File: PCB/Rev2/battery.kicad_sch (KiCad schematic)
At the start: 1 part, among them J2 Conn_01x04

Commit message: layout and  Routing adjustment
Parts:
- removed J2: Conn_01x04, 4ms_Connector:Pins_1x04_2.54mm_TH_SWD, symbol PCM_4ms_Connector:Conn_01x04
- added BT1, BT2: Battery, Connector_Molex:Molex_Panelmate_53780-0270_1x02-1MP_P1.25mm_Horizontal, symbol Device:Battery
- added C21: 10u, Capacitor_SMD:C_0402_1005Metric, symbol Device:C
- added C22: 22u, Capacitor_SMD:C_0603_1608Metric, symbol Device:C
- added L5: 2.2uH, Inductor_SMD:L_Changjiang_FNR252012S, symbol Device:L
- added R6: 1k, PCM_Resistor_SMD_AKL:R_0402_1005Metric, symbol Device:R
- added R7: 800k, PCM_Resistor_SMD_AKL:R_0603_1608Metric, symbol Device:R
- added R8: 10k, PCM_Resistor_SMD_AKL:R_0402_1005Metric, symbol Device:R
- added R9: 2M, PCM_Resistor_SMD_AKL:R_0603_1608Metric, symbol Device:R
- added U2: ETA6093, Package_TO_SOT_SMD:SOT-23-5, symbol ETA6093:ETA6093
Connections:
- net CHRG: now also R6.2, R8.1
- net GND: now also BT1.2 (-), BT2.2 (-), C21.2, C22.2, R9.2, U2.2 (GND)
- net VBUS: now also C22.1, R8.2, U2.1 (OUT)
- new net: L5.2, U2.5 (SW)
- new net: R6.1, U2.3 (LED)
- new net +BATT: BT1.1 (+), BT2.1 (+), C21.1, L5.1, R7.1, U2.4 (BAT)
- new net ADC: R7.2, R9.1
- no-connect marks 1 -> 0

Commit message: Change battery connector
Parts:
- BT1, BT2: footprint Connector_Molex:Molex_Panelmate_53780-0270_1x02-1MP_P1.25mm_Horizontal -> Connector_Molex:Molex_PicoBlade_53261-0271_1x02-1MP_P1.25mm_Horizontal
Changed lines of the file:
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@@
 			)
 		)
-		(property "Footprint" "Connector_Molex:Molex_Panelmate_53780-0270_1x02-1MP_P1.25mm_Horizontal"
+		(property "Footprint" "Connector_Molex:Molex_PicoBlade_53261-0271_1x02-1MP_P1.25mm_Horizontal"
 			(at 116.84 65.786 90)
 			(effects
@@
 			)
 		)
-		(property "Footprint" "Connector_Molex:Molex_Panelmate_53780-0270_1x02-1MP_P1.25mm_Horizontal"
+		(property "Footprint" "Connector_Molex:Molex_PicoBlade_53261-0271_1x02-1MP_P1.25mm_Horizontal"
 			(at 109.22 67.056 90)
 			(effects

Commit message: drc
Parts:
- removed BT1, BT2: Battery, Connector_Molex:Molex_PicoBlade_53261-0271_1x02-1MP_P1.25mm_Horizontal, symbol Device:Battery
- removed C21: 10u, Capacitor_SMD:C_0402_1005Metric, symbol Device:C
- removed C22: 22u, Capacitor_SMD:C_0603_1608Metric, symbol Device:C
- removed L5: 2.2uH, Inductor_SMD:L_Changjiang_FNR252012S, symbol Device:L
- removed R6: 1k, PCM_Resistor_SMD_AKL:R_0402_1005Metric, symbol Device:R
- removed R7: 800k, PCM_Resistor_SMD_AKL:R_0603_1608Metric, symbol Device:R
- removed R8: 10k, PCM_Resistor_SMD_AKL:R_0402_1005Metric, symbol Device:R
- removed R9: 2M, PCM_Resistor_SMD_AKL:R_0603_1608Metric, symbol Device:R
- removed U2: ETA6093, Package_TO_SOT_SMD:SOT-23-5, symbol ETA6093:ETA6093
- added BT3: Battery, Connector_Molex:Molex_PicoBlade_53261-0271_1x02-1MP_P1.25mm_Horizontal, symbol Device:Battery
- added C26: 20u, Capacitor_SMD:C_0402_1005Metric, symbol Device:C
- added C27: 10u, Capacitor_SMD:C_0402_1005Metric, symbol Device:C
- added C28: 22u, Capacitor_SMD:C_0603_1608Metric, symbol Device:C
- added L6: 2.2uH, Inductor_SMD:L_Changjiang_FNR252012S, symbol Device:L
- added R11: 1k, PCM_Resistor_SMD_AKL:R_0402_1005Metric, symbol Device:R
- added R12: 800k, PCM_Resistor_SMD_AKL:R_0603_1608Metric, symbol Device:R
- added R13: 2M, PCM_Resistor_SMD_AKL:R_0603_1608Metric, symbol Device:R
- added R14, R15: 10k, PCM_Resistor_SMD_AKL:R_0402_1005Metric, symbol Device:R
- added U4: LGS5500EP, Package_SO:SOIC-8-1EP_3.9x4.9mm_P1.27mm_EP2.41x3.3mm, symbol Battery_Management:LGS5500EP
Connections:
- net +BATT: now also BT3.1 (+), C28.1, L6.2, R12.2, U4.3 (VL)
- net ADC: now also R12.1, R13.2
- net CHRG: now also R15.1
- net GND: now also BT3.2 (-), C26.1, C27.2, C28.2, R11.1, R13.1, R14.2, U4.8 (NTC), U4.9 (GND)
- net VBUS: now also C26.2, U4.5 (VH)
- new net: R15.2, U4.7 (VSET/LED)
- new net: R14.1, U4.1 (ISET)
- new net: L6.1, U4.4 (LX)
- new net VBUS_USB: C27.1, R11.2, U4.2 (VIN)

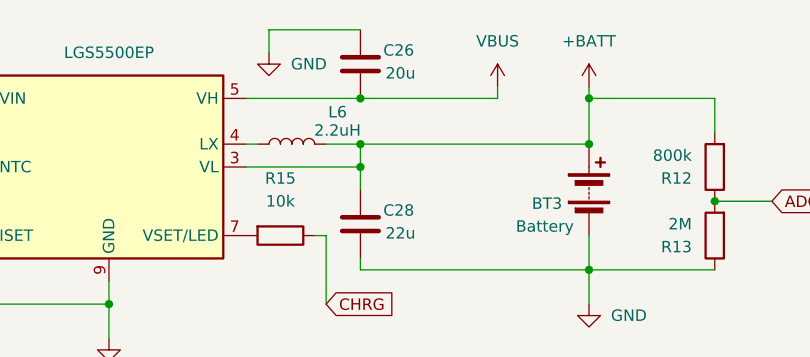
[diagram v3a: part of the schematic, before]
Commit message: Change charge and battery connector
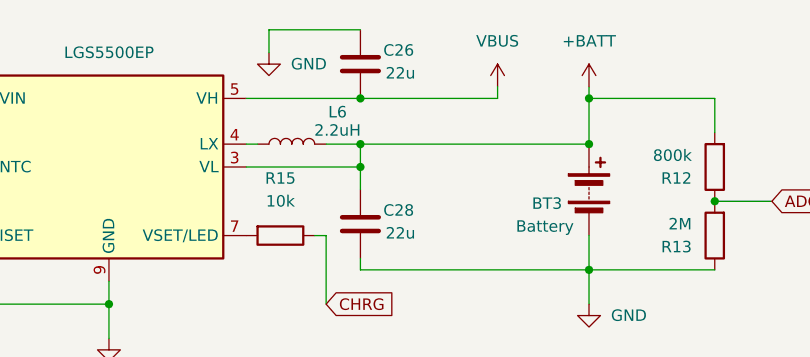
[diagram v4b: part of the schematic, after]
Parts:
- BT3: footprint Connector_Molex:Molex_PicoBlade_53261-0271_1x02-1MP_P1.25mm_Horizontal -> Connector_Molex:Molex_Panelmate_53780-0270_1x02-1MP_P1.25mm_Horizontal
- C26: value 20u -> 22u; footprint Capacitor_SMD:C_0402_1005Metric -> Capacitor_SMD:C_0603_1608Metric
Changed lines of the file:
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@@
 			)
 		)
-		(property "Footprint" "Connector_Molex:Molex_PicoBlade_53261-0271_1x02-1MP_P1.25mm_Horizontal"
+		(property "Footprint" "Connector_Molex:Molex_Panelmate_53780-0270_1x02-1MP_P1.25mm_Horizontal"
 			(at 165.1 67.056 90)
 			(effects
@@
 			)
 		)
-		(property "Value" "20u"
+		(property "Value" "22u"
 			(at 142.494 55.6259 0)
 			(effects
@@
 			)
 		)
-		(property "Footprint" "Capacitor_SMD:C_0402_1005Metric"
+		(property "Footprint" "Capacitor_SMD:C_0603_1608Metric"
 			(at 140.6652 58.42 0)
 			(effects

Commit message: Draft commit
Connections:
- net VBUS_USB is gone; now on net VBUS: C27.1, R11.2, U4.2 (VIN)
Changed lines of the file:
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@@
+	)
+	(junction
+		(at 81.28 58.42)
+		(diameter 0)
+		(color 0 0 0 0)
 	)
 	(junction
@@
 	)
 	(junction
+		(at 148.59 58.42)
+		(diameter 0)
+		(color 0 0 0 0)
+	)
+	(junction
 		(at 91.44 58.42)
 		(diameter 0)
@@
 	(wire
 		(pts
+			(xy 81.28 58.42) (xy 85.09 58.42)
+		)
+		(stroke
+			(width 0)
+			(type default)
+		)
+	)
+	(wire
+		(pts
 			(xy 129.54 50.8) (xy 139.7 50.8)
 		)
@@
 	(wire
 		(pts
-			(xy 72.39 52.07) (xy 72.39 58.42)
+			(xy 66.04 50.8) (xy 66.04 58.42)
 		)
 		(stroke
@@
 	(wire
 		(pts
+			(xy 148.59 58.42) (xy 154.94 58.42)
+		)
+		(stroke
+			(width 0)
+			(type default)
+		)
+	)
+	(wire
+		(pts
 			(xy 179.07 77.47) (xy 165.1 77.47)
 		)
@@
 	(wire
 		(pts
-			(xy 139.7 58.42) (xy 154.94 58.42)
+			(xy 139.7 58.42) (xy 148.59 58.42)
 		)
 		(stroke
@@
 	(wire
 		(pts
-			(xy 72.39 58.42) (xy 85.09 58.42)
+			(xy 66.04 58.42) (xy 81.28 58.42)
 		)
 		(stroke
@@
 	(wire
 		(pts
+			(xy 81.28 48.26) (xy 148.59 48.26)
+		)
+		(stroke
+			(width 0)
+			(type default)
+		)
+	)
+	(wire
+		(pts
 			(xy 154.94 58.42) (xy 154.94 57.15)
 		)
@@
 	(wire
 		(pts
+			(xy 148.59 48.26) (xy 148.59 58.42)
+		)
+		(stroke
+			(width 0)
+			(type default)
+		)
+	)
+	(wire
+		(pts
 			(xy 179.07 62.23) (xy 179.07 58.42)
 		)
@@
 		(pts
 			(xy 91.44 66.04) (xy 96.52 66.04)
+		)
+		(stroke
+			(width 0)
+			(type default)
+		)
+	)
+	(wire
+		(pts
+			(xy 81.28 48.26) (xy 81.28 58.42)
 		)
 		(stroke
@@
 	(symbol
 		(lib_id "power:VBUS")
-		(at 72.39 52.07 0)
+		(at 66.04 50.8 0)
 		(unit 1)
 		(exclude_from_sim no)
@@
 		(fields_autoplaced yes)
 		(property "Reference" "#PWR037"
-			(at 72.39 55.88 0)
+			(at 66.04 54.61 0)
 			(effects
 				(font
@@
 		)
 		(property "Value" "VBUS_USB"
-			(at 74.93 50.7999 0)
+			(at 68.58 49.5299 0)
 			(effects
 				(font
@@
 		)
 		(property "Footprint" ""
-			(at 72.39 52.07 0)
+			(at 66.04 50.8 0)
 			(effects
 				(font
@@
 		)
 		(property "Datasheet" ""
-			(at 72.39 52.07 0)
+			(at 66.04 50.8 0)
 			(effects
 				(font
@@
 		)
 		(property "Description" "Power symbol creates a global label with name \"VBUS\""
-			(at 72.39 52.07 0)
-			(effects
-				(font
+			(at 66.04 50.8 0)
+			(effects
+				(font

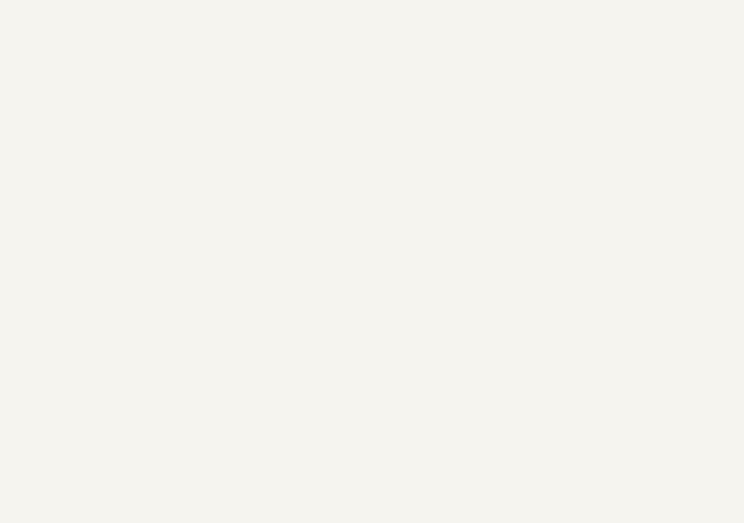
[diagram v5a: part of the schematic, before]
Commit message: LP7801D封装绘制与原理图导入
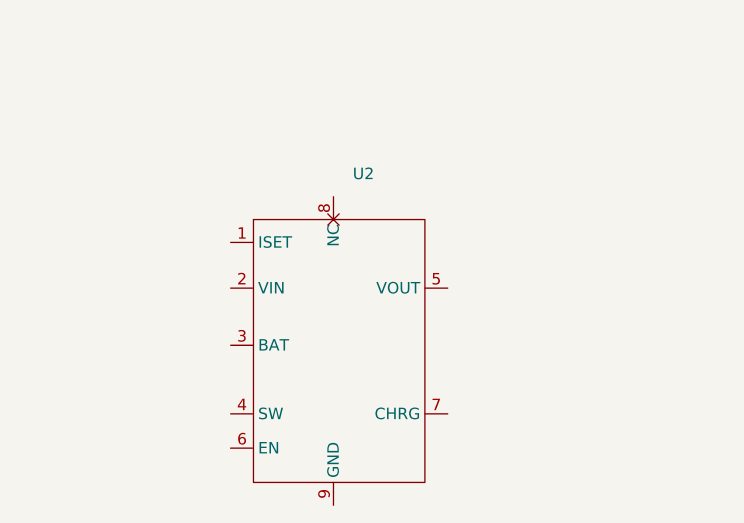
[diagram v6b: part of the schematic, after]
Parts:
- added U2: ~, Package_SO:SOP-8-1EP_4.57x4.57mm_P1.27mm_EP4.57x4.45mm, symbol LP7801D_sym:LP7801D
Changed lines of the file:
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@@
+	)
+	(symbol
+		(lib_id "LP7801D_sym:LP7801D")
+		(at 85.09 113.03 0)
+		(unit 1)
+		(exclude_from_sim no)
+		(in_bom yes)
+		(on_board yes)
+		(dnp no)
+		(fields_autoplaced yes)
+		(property "Reference" "U2"
+			(at 102.4733 113.03 0)
+			(effects
+				(font
+					(size 1.27 1.27)
+				)
+				(justify left)
+			)
+		)
+		(property "Value" "~"
+			(at 102.4733 115.57 0)
+			(effects
+				(font
+					(size 1.27 1.27)
+				)
+				(justify left)
+			)
+		)
+		(property "Footprint" "Package_SO:SOP-8-1EP_4.57x4.57mm_P1.27mm_EP4.57x4.45mm"
+			(at 96.774 157.988 0)
+			(effects
+				(font
+					(size 1.27 1.27)
+				)
+				(hide yes)
+			)
+		)
+		(property "Datasheet" ""
+			(at 85.09 113.03 0)
+			(effects
+				(font
+					(size 1.27 1.27)
+				)
+				(hide yes)
+			)
+		)
+		(property "Description" ""
+			(at 85.09 113.03 0)
+			(effects
+				(font
+					(size 1.27 1.27)
+				)
+				(hide yes)
+			)
+		)
+		(pin "1"
+		)
+		(pin "2"
+		)
+		(pin "4"
+		)
+		(pin "8"
+		)
+		(pin "3"
+		)
+		(pin "6"
+		)
+		(pin "9"
+		)
+		(pin "5"
+		)
+		(pin "7"
+		)
+		(instances
+			(project ""
+				(path "/dca0f898-8fdb-4522-a51d-f4f4238906e7/65afedf5-5b27-4d53-9ad9-9264a927261c"
+					(reference "U2")
+					(unit 1)
+				)
+			)
+		)
 	)
 	(symbol

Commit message: LP7801D设计（封装未审核）
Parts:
- removed U2: ~, Package_SO:SOP-8-1EP_4.57x4.57mm_P1.27mm_EP4.57x4.45mm, symbol LP7801D_sym:LP7801D
- added C21, C22: 10u, Capacitor_SMD:C_0402_1005Metric, symbol Device:C
- added L5: 2.2uH, Inductor_SMD:L_Changjiang_FNR252012S, symbol Device:L
- added R8: 10k, PCM_Resistor_SMD_AKL:R_0402_1005Metric, symbol Device:R
- added U3: ~, Package_SO:SOP-8-1EP_4.57x4.57mm_P1.27mm_EP4.57x4.45mm, symbol LP7801D_sym:LP7801D
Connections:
- net VBUS is gone; now on net +BATT: C26.2, C27.1, R11.2, U4.2 (VIN), U4.5 (VH)
- net +BATT: now also C21.1, L5.2, U3.2 (VIN), U3.3 (BAT)
- net GND: now also C21.2, C22.2, R8.2, U3.9 (GND)
- new net: R8.1, U3.1 (ISET)
- new net: L5.1, U3.4 (SW)
- new net LP7801_EN: U3.6 (EN)
- new net RGB_VDD: C22.1, U3.5 (VOUT)
- no-connect marks 0 -> 2
